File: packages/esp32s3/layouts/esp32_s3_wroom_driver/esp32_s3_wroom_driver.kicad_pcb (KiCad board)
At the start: 2 copper layers, 7 parts

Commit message: Rebuild all
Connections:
- U2 pad 10: line-25 -> line-33
- U2 pad 11: line-18 -> line-21
- U2 pad 13: line -> line-14
- U2 pad 14: line-29 -> line-24
- U2 pad 15: line-31 -> line-10
- U2 pad 16: line-5 -> line-11
- U2 pad 17: line-12 -> line-8
- U2 pad 19: line-3 -> line-23
- U2 pad 20: line-9 -> line-13
- U2 pad 21: line-7 -> line-15
- U2 pad 22: line-16 -> line-1
- U2 pad 23: line-32 -> line-25
- U2 pad 24: line-2 -> line-29
- U2 pad 25: line-20 -> line-27
- U2 pad 26: line-4 -> line-28
- U2 pad 28: line-6 -> line-18
- U2 pad 29: line-22 -> line
- U2 pad 30: line-1 -> line-30
- U2 pad 31: line-15 -> line-6
- U2 pad 32: line-11 -> line-5
- U2 pad 33: line-14 -> line-17
- U2 pad 34: line-19 -> line-7
- U2 pad 35: line-30 -> line-12
- U2 pad 36: line-8 -> line-4
- U2 pad 37: line-17 -> line-31
- U2 pad 38: line-10 -> line-20
- U2 pad 39: line-23 -> line-32
- U2 pad 4: line-21 -> line-9
- U2 pad 5: line-13 -> line-22
- U2 pad 6: line-24 -> line-16
- U2 pad 7: line-33 -> line-3
- U2 pad 8: line-28 -> line-2
- U2 pad 9: line-27 -> line-19

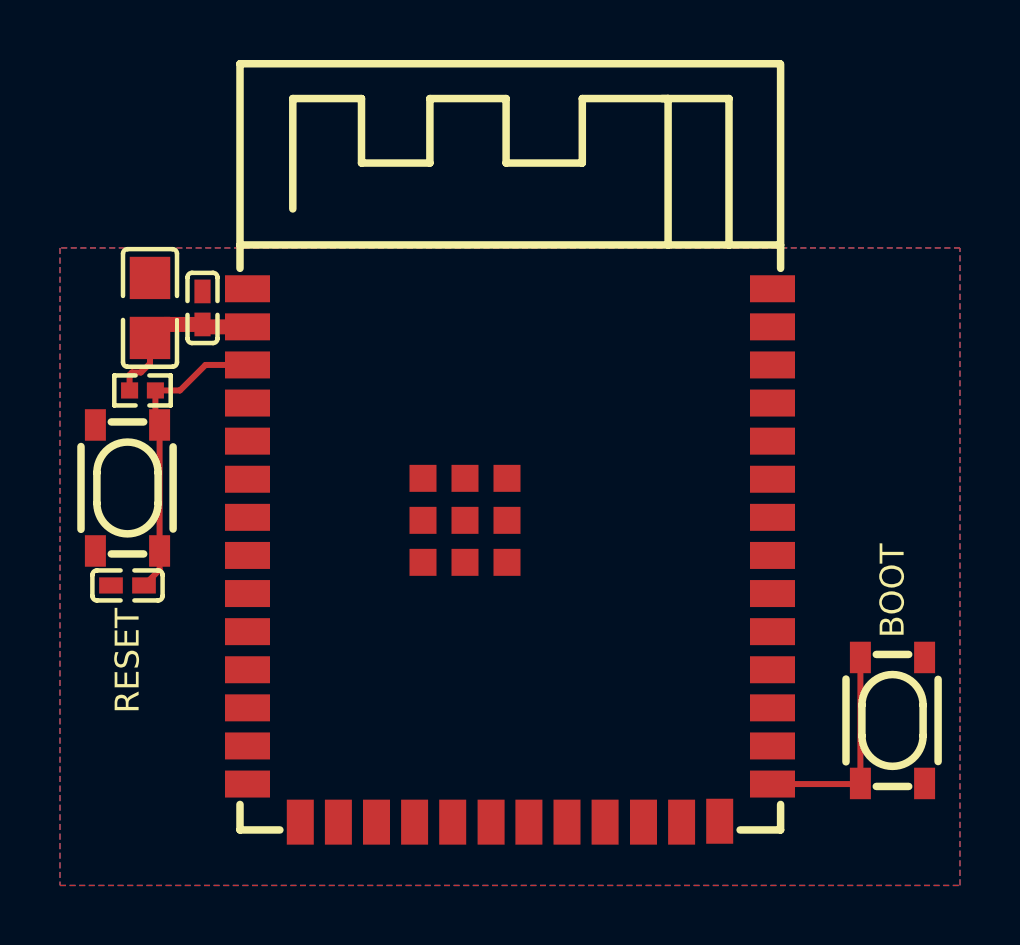
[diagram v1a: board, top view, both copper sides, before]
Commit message: Manually fix fp lib tables
fix some small bugs
fix package only modules (e.g. logos)
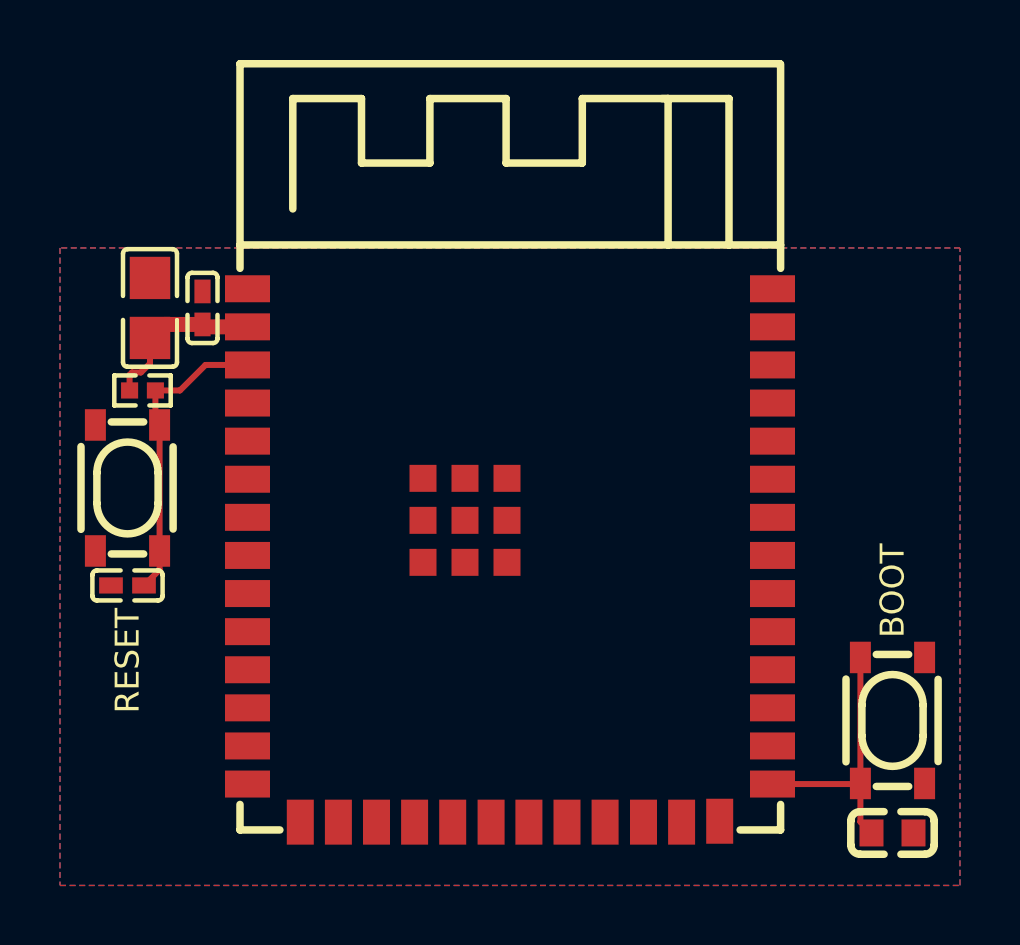
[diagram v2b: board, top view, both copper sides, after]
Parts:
- added C4: 100nF ±10% 50V X7R, YAGEO_CC0603KRX7R9BB104:C0603, F.Cu at (12.8, 9.25)
- C1: footprint atopile:C0805-3b2e55 -> YAGEO_CC0805KRX7R9BB104:C0805
- C2, C3: footprint atopile:C0402-b3ef17 -> Samsung_Electro_Mechanics_CL05B104KO5NNNC:C0402
- R1: footprint atopile:R0402-56259e -> UNI_ROYAL_0402WGF1002TCE:R0402
- U1, U3: footprint lib:KEY-SMD_4P-L4.2-W3.2-P2.20-LS4.6 -> ALPSALPINE_SKRPACE010:KEY-SMD_4P-L4.2-W3.2-P2.20-LS4.6
- U2: footprint atopile:WIRELM-SMD_ESP32-S3-WROOM-1-41522d -> Espressif_Systems_ESP32_S3_WROOM_1_N16R2:WIRELM-SMD_ESP32-S3-WROOM-1
- turned R1 to 180 degrees
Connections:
- C3 pad 1: input -> line-32
- R1 pad 1: hv -> line-32
- R1 pad 2: input -> hv
- U1 pad 3: output -> line-16
- U1 pad 4: output -> line-16
- U2 pad 10: line-33 -> line-19
- U2 pad 11: line-21 -> line-5
- U2 pad 12: line-26 -> line-33
- U2 pad 13: line-14 -> line-35
- U2 pad 14: line-24 -> line-10
- U2 pad 15: line-10 -> line-3
- U2 pad 16: line-11 -> line-6
- U2 pad 17: line-8 -> line-24
- U2 pad 18: line-34 -> line-18
- U2 pad 19: line-23 -> line-29
- U2 pad 20: line-13 -> line-31
- U2 pad 21: line-15 -> line-14
- U2 pad 22: line-1 -> line-2
- U2 pad 23: line-25 -> line-23
- U2 pad 24: line-29 -> line-30
- U2 pad 25: line-27 -> line-4
- U2 pad 26: line-28 -> line-12
- U2 pad 27: output -> line-16
- U2 pad 28: line-18 -> line-1
- U2 pad 29: line -> line-25
- U2 pad 3: input -> line-32
- U2 pad 30: line-30 -> line-15
- U2 pad 31: line-6 -> line-28
- U2 pad 32: line-5 -> line-27
- U2 pad 33: line-17 -> line-7
- U2 pad 34: line-7 -> line-34
- U2 pad 35: line-12 -> line-13
- U2 pad 36: line-4 -> line-8
- U2 pad 37: line-31 -> line-17
- U2 pad 38: line-20 -> line-21
- U2 pad 39: line-32 -> line
- U2 pad 4: line-9 -> line-11
- U2 pad 5: line-22 -> line-20
- U2 pad 6: line-16 -> line-36
- U2 pad 7: line-3 -> line-22
- U2 pad 8: line-2 -> line-9
- U2 pad 9: line-19 -> line-26
- U3 pad 1: input -> line-32
- U3 pad 2: input -> line-32
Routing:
- net line-32: track 0.00 -> 10.2 mm
- net input: track 10.2 -> 0.00 mm
- net line-16: track 0.00 -> 8.94 mm
- net output: track 7.14 -> 0.00 mm

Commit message: Update 3D model locations
fix missing renders
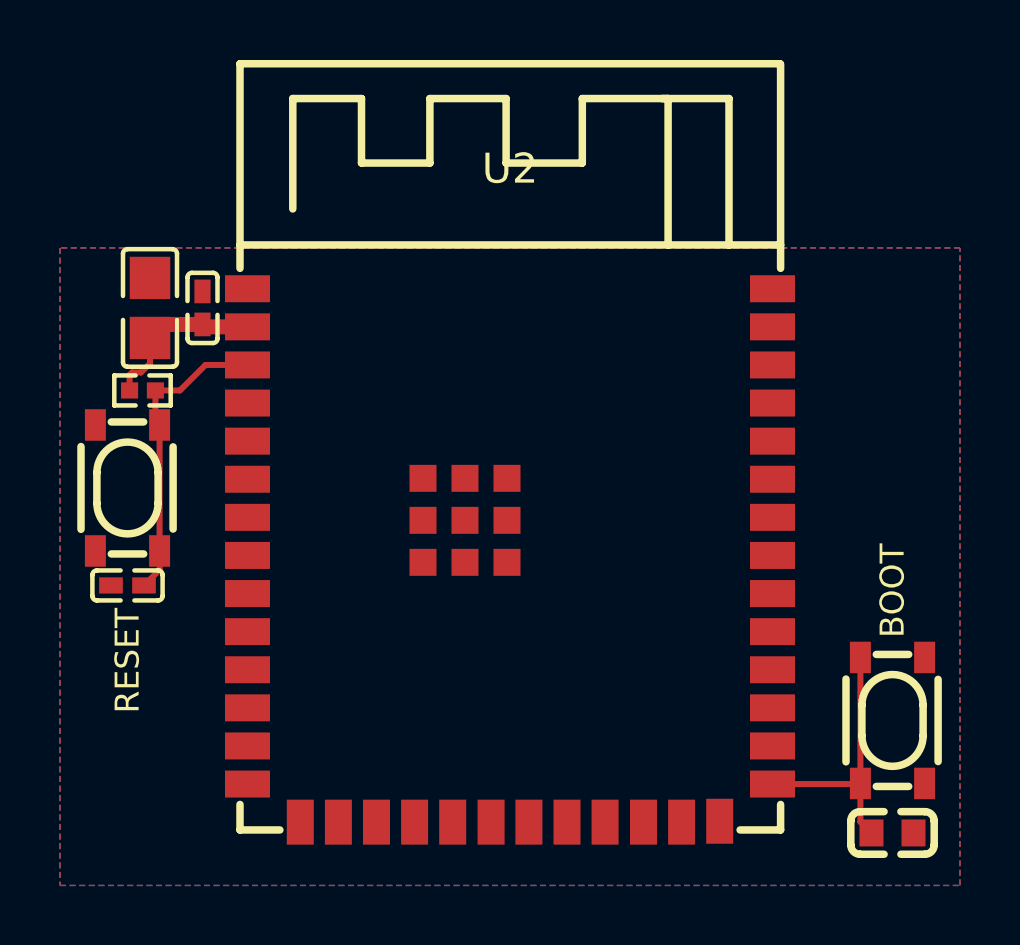
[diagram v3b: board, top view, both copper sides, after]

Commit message: rebuild all packages & regenerate images of changed layouts (silk)
Add new scripts for version bump and build (based on atopile/packages)
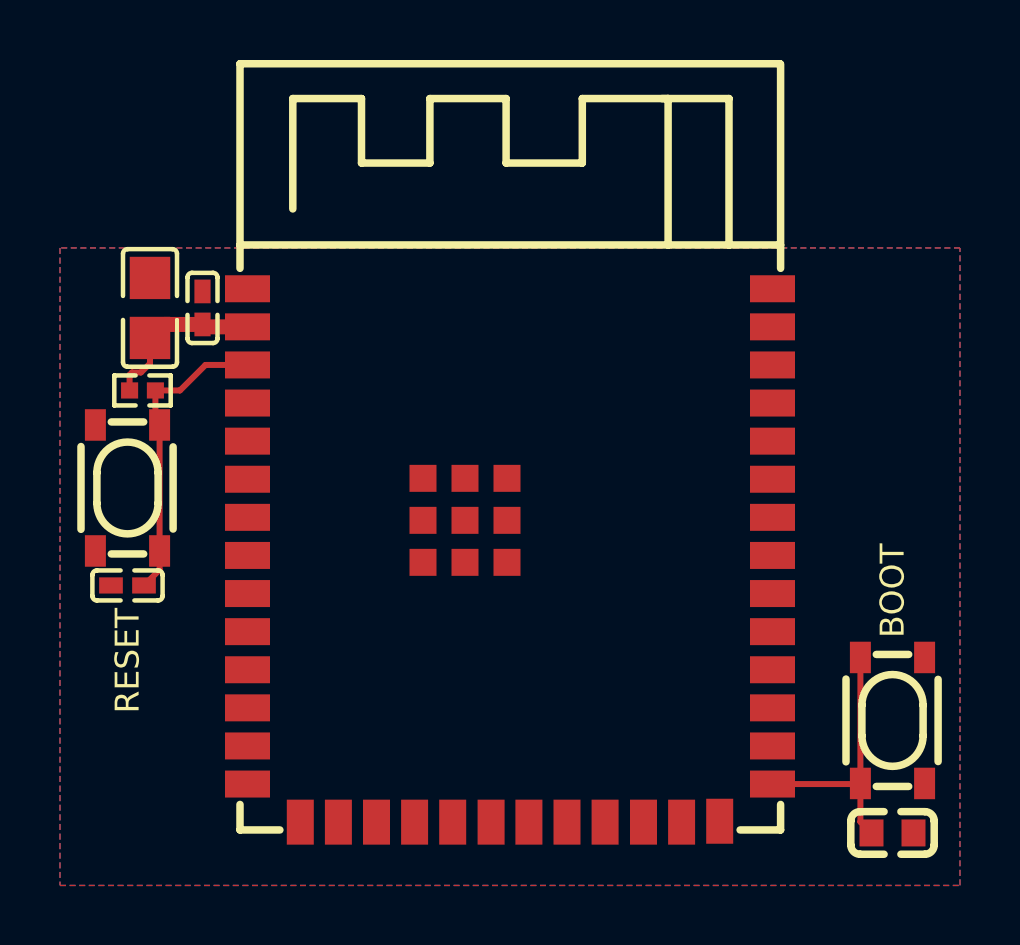
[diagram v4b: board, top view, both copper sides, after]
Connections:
- C3 pad 1: line-32 -> line
- C4 pad 1: line-16 -> line-1
- R1 pad 1: line-32 -> line
- U1 pad 3: line-16 -> line-1
- U1 pad 4: line-16 -> line-1
- U2 pad 10: line-19 -> line-9
- U2 pad 11: line-5 -> line-10
- U2 pad 12: line-33 -> line-35
- U2 pad 13: line-35 -> line-11
- U2 pad 14: line-10 -> line-13
- U2 pad 15: line-3 -> line-21
- U2 pad 16: line-6 -> line-28
- U2 pad 17: line-24 -> line-36
- U2 pad 18: line-18 -> line-2
- U2 pad 19: line-29 -> line-3
- U2 pad 20: line-31 -> line-4
- U2 pad 21: line-14 -> line-5
- U2 pad 22: line-2 -> line-6
- U2 pad 23: line-23 -> line-14
- U2 pad 24: line-30 -> line-29
- U2 pad 25: line-4 -> line-30
- U2 pad 26: line-12 -> line-27
- U2 pad 27: line-16 -> line-1
- U2 pad 28: line-1 -> line-16
- U2 pad 29: line-25 -> line-17
- U2 pad 3: line-32 -> line
- U2 pad 30: line-15 -> line-18
- U2 pad 31: line-28 -> line-19
- U2 pad 32: line-27 -> line-20
- U2 pad 33: line-7 -> line-22
- U2 pad 34: line-34 -> line-23
- U2 pad 35: line-13 -> line-24
- U2 pad 36: line-8 -> line-25
- U2 pad 37: line-17 -> line-26
- U2 pad 38: line-21 -> line-15
- U2 pad 39: line -> line-12
- U2 pad 4: line-11 -> line-31
- U2 pad 5: line-20 -> line-32
- U2 pad 6: line-36 -> line-33
- U2 pad 7: line-22 -> line-34
- U2 pad 8: line-9 -> line-7
- U2 pad 9: line-26 -> line-8
- U3 pad 1: line-32 -> line
- U3 pad 2: line-32 -> line
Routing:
- net line-32: track 10.2 -> 0.00 mm
- net line: track 0.00 -> 10.2 mm
- net line-16: track 8.94 -> 0.00 mm
- net line-1: track 0.00 -> 8.94 mm
